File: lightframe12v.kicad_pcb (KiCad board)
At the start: 2 copper layers, 91.4 x 45.7 mm, 46 parts, among them J1 PJ-077, J2 Conn_01x06_Female, J3 Conn_01x06_Female, J4 Conn_01x04_Female, J5 Conn_01x6_Female, Q1 MMBT2222, Q2 MMBT2222, SW1 SW_Push, SW2 SW_Push, U1 ESP32-WROOM-32U, U2 TPS563207s, U3 TLC5971

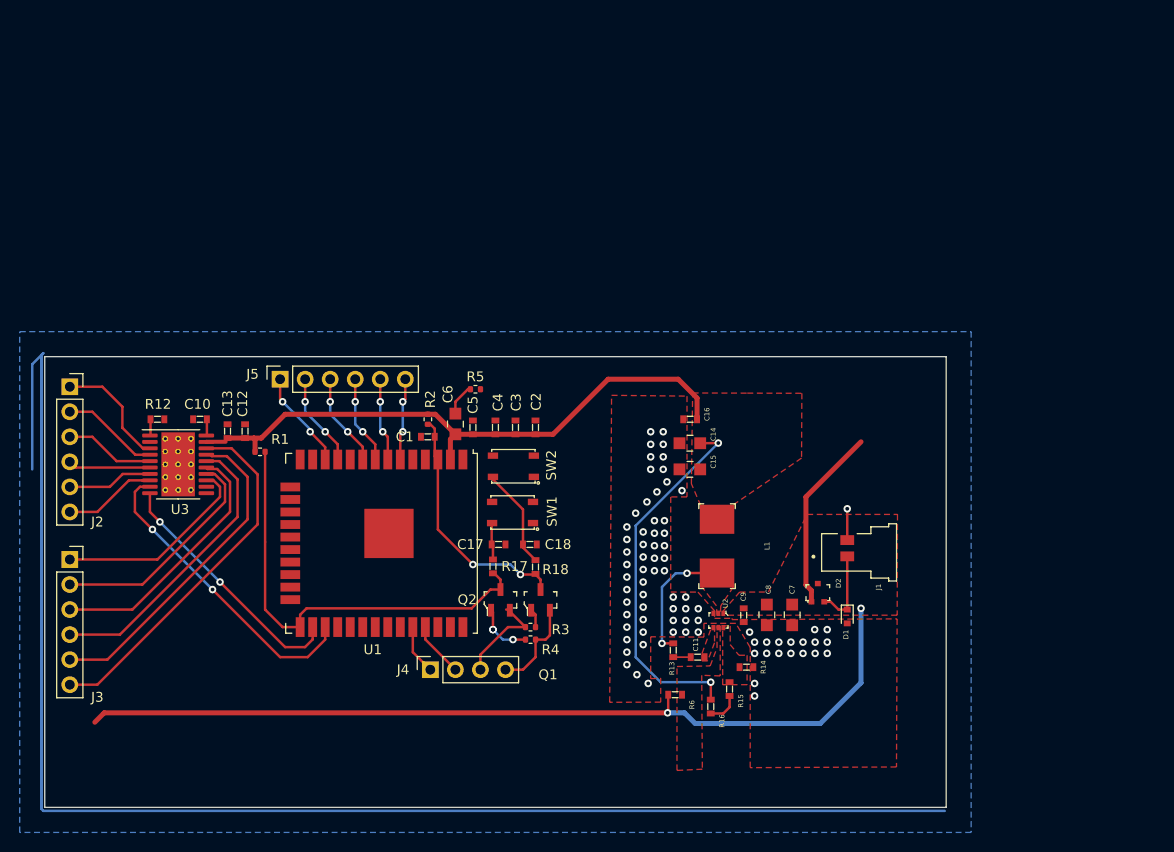
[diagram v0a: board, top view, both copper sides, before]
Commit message: Created pmic footprint
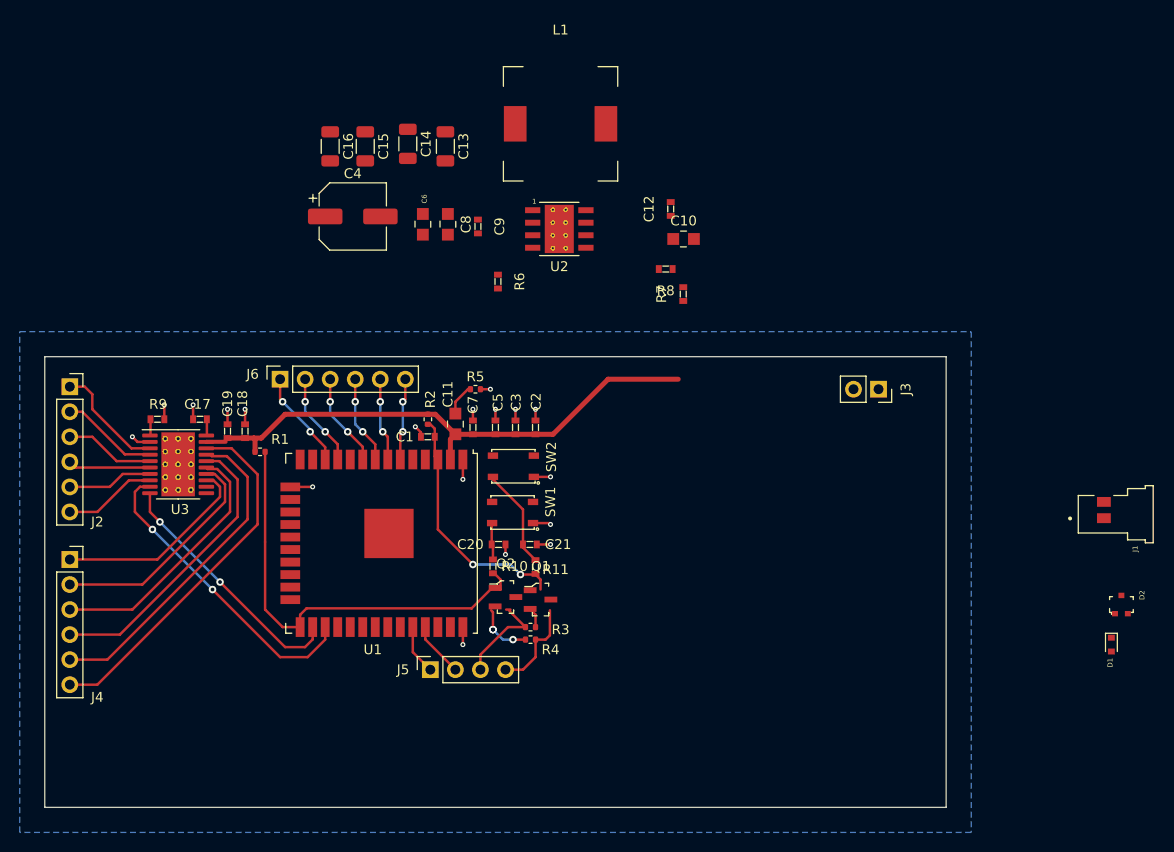
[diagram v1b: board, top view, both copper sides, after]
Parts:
- removed the C11 at (338.0, -508.0)
- removed the C7 at (347.6, -512.3)
- removed R13: 0k, digikey-footprints:0603
- removed R14: 10k, digikey-footprints:0603
- removed R15: 30.9k, digikey-footprints:0603
- removed R16: 51, digikey-footprints:0603
- added C10: 1uF, digikey-footprints:0805, F.Cu at (336.6, -550.4)
- added C12: .1uF, digikey-footprints:0603, F.Cu at (335.3, -553.5)
- added C13: 22uF, Capacitor_SMD:C_1206_3216Metric, F.Cu at (312.4, -559.8)
- added C4: 100uF AL, Capacitor_SMD:CP_Elec_6.3x5.4, F.Cu at (303.0, -552.7)
- added C9: .1uF, digikey-footprints:0603, F.Cu at (315.7, -551.7)
- added J3: Conn_01x02_Female, Connector_PinSocket_2.54mm:PinSocket_1x02_P2.54mm_Vertical, F.Cu at (356.4, -535.2)
- added R7: 100k, digikey-footprints:0603, F.Cu at (336.6, -544.8)
- added R8: 43.2k, digikey-footprints:0603, F.Cu at (334.8, -547.4)
- C14, C15: footprint digikey-footprints:0805 -> Capacitor_SMD:C_1206_3216Metric
- C16: value 100nF -> 22uF; footprint digikey-footprints:0603 -> Capacitor_SMD:C_1206_3216Metric
- C6: renamed from C8; value 10uF -> 4.7uF
- C8: renamed from C9; value 100nF -> 4.7uF; footprint digikey-footprints:0603 -> digikey-footprints:0805
- L1: value 1.2uH -> 8.2uH; footprint keith:Wurth 74437349012 Inductor -> Keith:wurth 7443330820 8.2uH
- Q1, Q2: value MMBT2222 -> MMBT2222A-TP
- U2: value TPS563207s -> LMR33620Simple; footprint digikey-footprints:SOT-563 -> Keith:lmr33620HSOIC
- moved C6 52.8 mm to (310.1, -551.9)
- moved C8 49.7 mm to (312.7, -551.9)
- moved C15 46.5 mm to (304.3, -559.8), turned to 270 degrees
- moved C16 45.8 mm to (300.7, -559.8), turned to 270 degrees
- moved L1 45.7 mm to (324.1, -562.1), turned to 180 degrees
- moved R6 45.6 mm to (317.8, -546.1), turned to 270 degrees
- moved U2 42.9 mm to (324.0, -551.4), turned to 0 degrees
- moved C14 41.7 mm to (308.6, -560.1), turned to 270 degrees
- moved D2 30.8 mm to (381.0, -513.3)
- moved D1 26.9 mm to (380.0, -509.3)
- moved J1 26.3 mm to (380.5, -522.5)
- moved Q2 0.58 mm to (318.5, -514.1), turned to 0 degrees
- turned Q1 to 0 degrees
- renumbered C6 to C11, C10 to C17, C12 to C18, C13 to C19, C17 to C20, C18 to C21, C4 to C5, C5 to C7, J3 to J4, J4 to J5, J5 to J6, R17 to R10, R18 to R11, R12 to R9
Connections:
- C14 pad 2: GND -> Net-(C13-Pad2)
- C15 pad 2: GND -> Net-(C13-Pad2)
- C16 pad 2: GND -> Net-(C13-Pad2)
- C6 pad 1: +12V -> +24V
- C8 pad 1: +12V -> +24V
- D2 pad 1: +12V -> +24V
- L1 pad 1: Net-(L1-Pad1) -> Net-(C12-Pad2)
- Q2 pad 2: /Dtr -> /Gpio0
- Q2 pad 3: /Gpio0 -> /Dtr
- R6 pad 1: +12V -> Net-(R6-Pad1)
- R6 pad 2: Net-(R6-Pad2) -> GND
- U2 pad 1: +12V -> GND
- U2 pad 2: Net-(L1-Pad1) -> +24V
- U2 pad 3: GND -> +24V
- U2 pad 4: Net-(C11-Pad1) -> Net-(R6-Pad1)
- U2 pad 5: Net-(R6-Pad2) -> GND
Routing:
- net (no net): track 196.3 -> 0.00 mm
- net +12V: track 108.4 -> 0.00 mm, vias 2 -> 0
- net +3V3: track 99.3 -> 56.1 mm, vias 2 -> 0
- net GND: track 3.18 -> 26.8 mm, vias 78 -> 18
- net Net-(L1-Pad1): track 13.2 -> 0.00 mm, vias 2 -> 0
- net Net-(D1-Pad1): track 8.06 -> 0.00 mm
- net Net-(R15-Pad2): track 3.31 -> 0.00 mm
- net Net-(C11-Pad2) (its old number): track 1.78 -> 0.00 mm
- removed copper zone on F.Cu, net +12V
- removed copper zone on F.Cu, net +3V3
- removed copper zone on F.Cu, net GND
- removed copper zone on F.Cu, net Net-(C10-Pad1)
- removed copper zone on F.Cu, net Net-(C11-Pad1)
- removed copper zone on F.Cu, net Net-(L1-Pad1)
- removed copper zone on F.Cu, net Net-(R6-Pad2)

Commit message: Rough layout of pmic
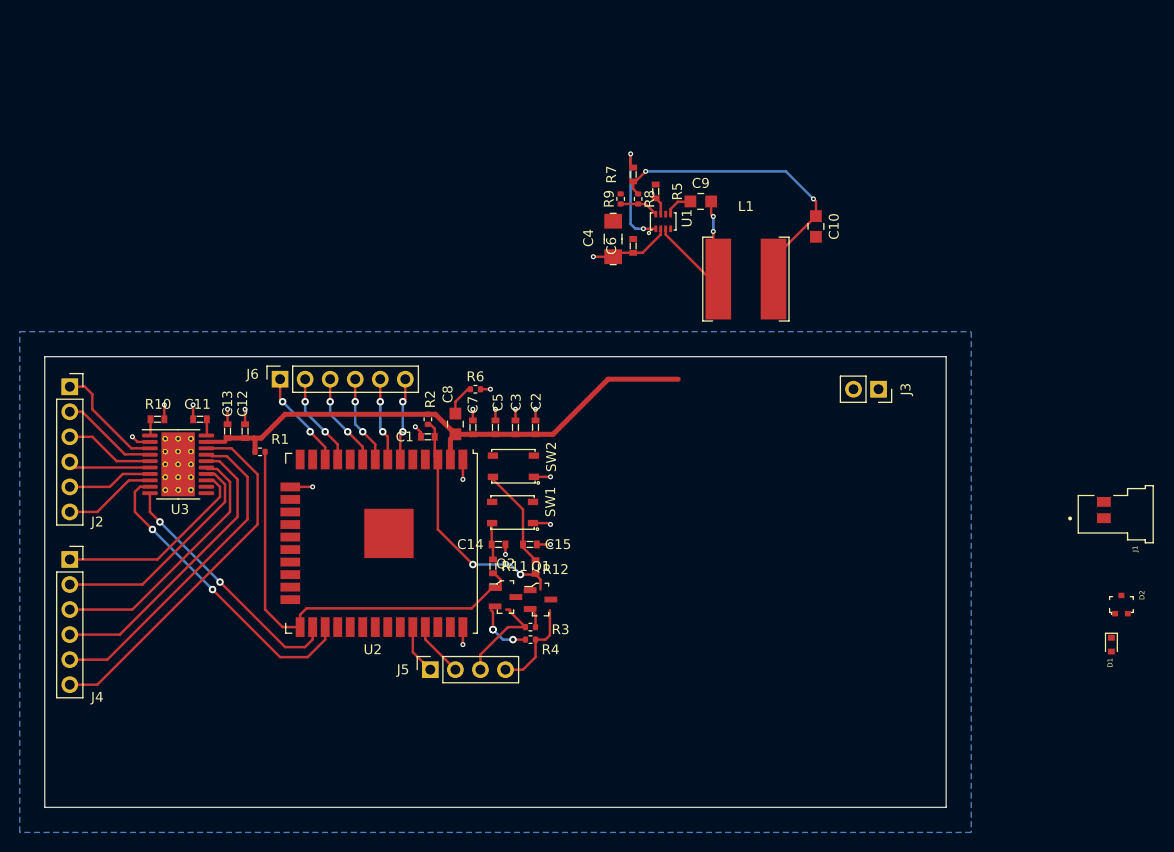
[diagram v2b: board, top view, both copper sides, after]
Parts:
- removed the C12 at (335.3, -553.5)
- removed the C13 at (312.4, -559.8)
- removed the C14 at (308.6, -560.1)
- removed the C15 at (304.3, -559.8)
- removed C16: 22uF, Capacitor_SMD:C_1206_3216Metric
- removed the C4 at (303.0, -552.7)
- removed the C6 at (310.1, -551.9)
- removed the R8 at (334.8, -547.4)
- removed the U2 at (324.0, -551.4)
- added C9: 100nF, digikey-footprints:0805, F.Cu at (338.3, -554.2)
- added R5: 0, digikey-footprints:0603, F.Cu at (333.8, -555.2)
- added R9: 10k, Resistor_SMD:R_0402_1005Metric, F.Cu at (330.2, -554.5)
- added U1: TPS562211, Keith:TPS562211 12V pmic, F.Cu at (334.5, -552.2)
- C10: value 1uF -> 22uF
- C4: renamed from C8; value 4.7uF -> 22uF; footprint digikey-footprints:0805 -> digikey-footprints:1206
- C6: renamed from C9; value .1uF -> 100nF
- L1: value 8.2uH -> 4.7uH; footprint Keith:wurth 7443330820 8.2uH -> Keith:SRN8040 Bournes
- R7: renamed from R6; value 20k -> 10k
- R8: renamed from R7; value 100k -> 45.3k; footprint digikey-footprints:0603 -> Resistor_SMD:R_0402_1005Metric
- moved L1 24.5 mm to (342.9, -546.4), turned to 0 degrees
- moved R7 17.5 mm to (331.5, -557.0), turned to 90 degrees
- moved C4 16.8 mm to (329.4, -550.4), turned to 90 degrees
- moved C6 15.9 mm to (331.5, -549.7), turned to 90 degrees
- moved C10 13.5 mm to (350.0, -551.7), turned to 270 degrees
- moved R8 10.7 mm to (332.0, -554.5), turned to 270 degrees
- renumbered C17 to C11, C18 to C12, C19 to C13, C20 to C14, C21 to C15, C11 to C8, R9 to R10, R10 to R11, R11 to R12, R5 to R6, U1 to U2
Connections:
- net +24V renamed +12V
- C10 pad 1: Net-(C10-Pad1) -> +3V3
- R7 pad 1: Net-(R6-Pad1) -> +3V3
- R7 pad 2: GND -> Net-(R7-Pad2)
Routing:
- net +3V3: track 56.1 -> 87.5 mm, vias 0 -> 2
- net Net-(C9-Pad2): track 0.00 -> 17.0 mm, vias 0 -> 2
- net Net-(R7-Pad2): track 0.00 -> 11.2 mm, vias 0 -> 2
- net +12V: track 0.00 -> 8.36 mm, vias 0 -> 1
- net Net-(R8-Pad2): track 0.00 -> 4.00 mm
- net Net-(C9-Pad1): track 0.00 -> 2.61 mm
- net Net-(R5-Pad2): track 0.00 -> 1.82 mm

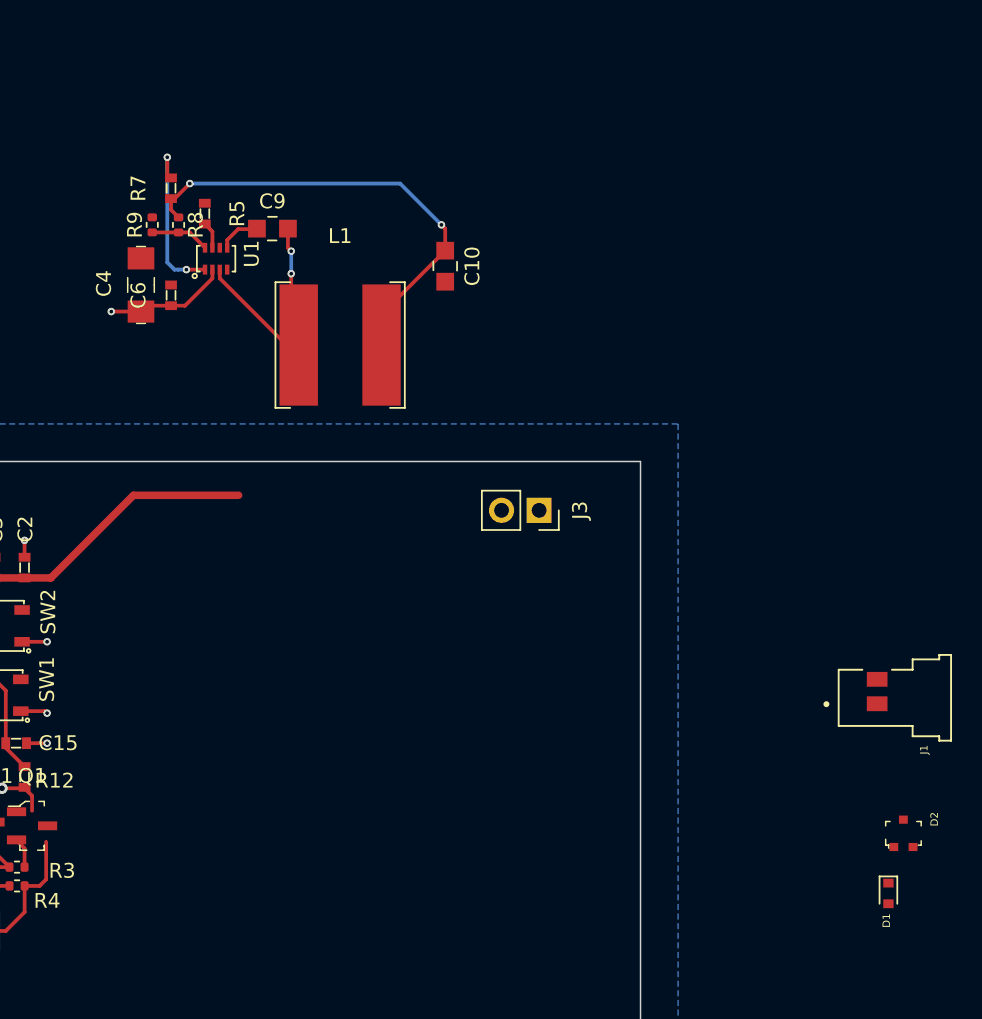
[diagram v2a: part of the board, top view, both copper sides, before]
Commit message: Pmic zones
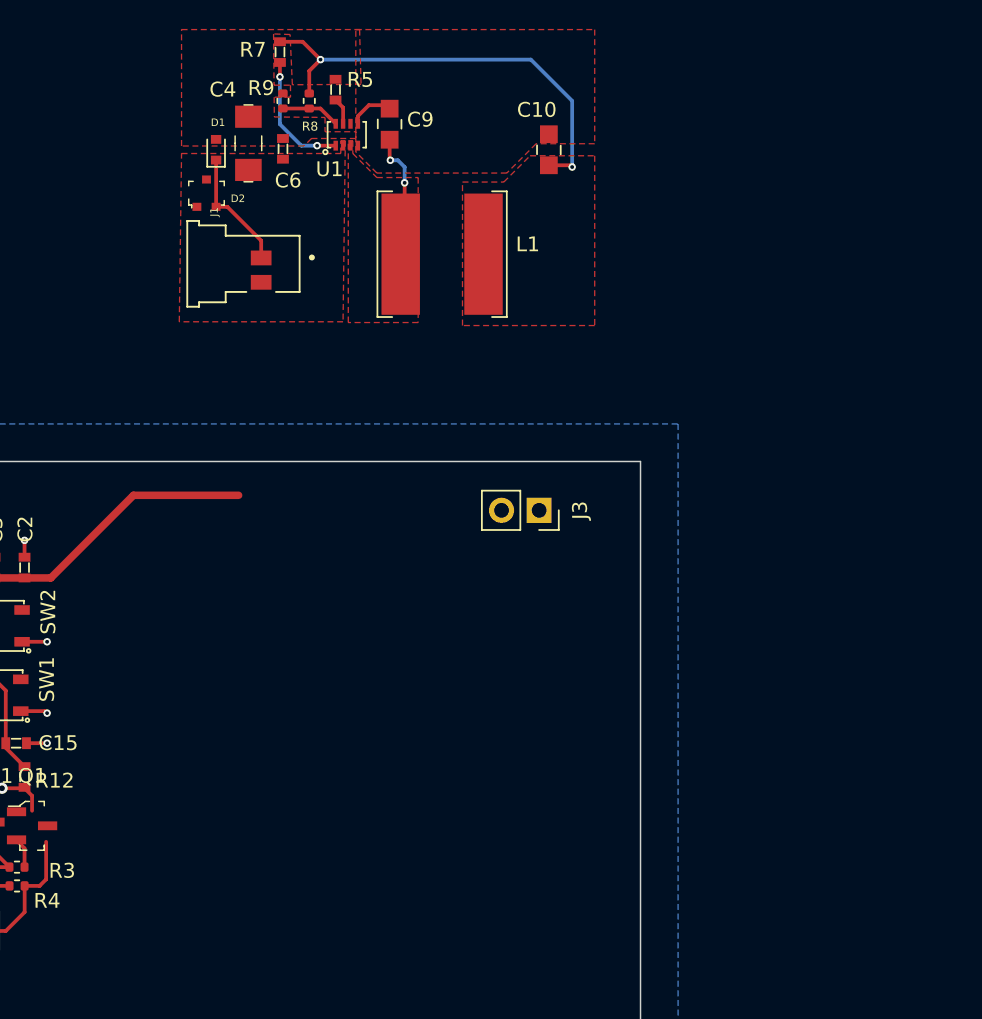
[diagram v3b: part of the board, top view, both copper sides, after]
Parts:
- moved D1 67.8 mm to (334.5, -559.6), turned to 90 degrees
- moved D2 64.0 mm to (333.9, -556.6)
- moved J1 53.1 mm to (336.3, -551.8), turned to 180 degrees
- moved C6 12.5 mm to (339.0, -559.6)
- moved R5 12.2 mm to (342.6, -563.6)
- moved R8 12.2 mm to (340.8, -562.9)
- moved U1 12.2 mm to (343.4, -560.6)
- moved R9 12.2 mm to (339.0, -562.9)
- moved C4 12.0 mm to (336.7, -560.0)
- moved R7 11.8 mm to (338.8, -566.2), turned to 270 degrees
- moved C9 10.6 mm to (346.3, -561.3), turned to 270 degrees
- moved C10 10.5 mm to (357.0, -559.6), turned to 90 degrees
- moved L1 9.24 mm to (349.8, -552.5)
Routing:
- net Net-(C9-Pad2): track 17.0 -> 8.57 mm
- net +12V: track 8.36 -> 0.00 mm, vias 1 -> 0
- net Net-(D1-Pad1): track 0.00 -> 8.32 mm
- net Net-(R7-Pad2): track 11.2 -> 8.55 mm
- net +3V3: track 87.5 -> 86.2 mm
- added copper zone on F.Cu, net +12V
- added copper zone on F.Cu, net +3V3
- added copper zone on F.Cu, net GND
- added copper zone on F.Cu, net Net-(C9-Pad2)

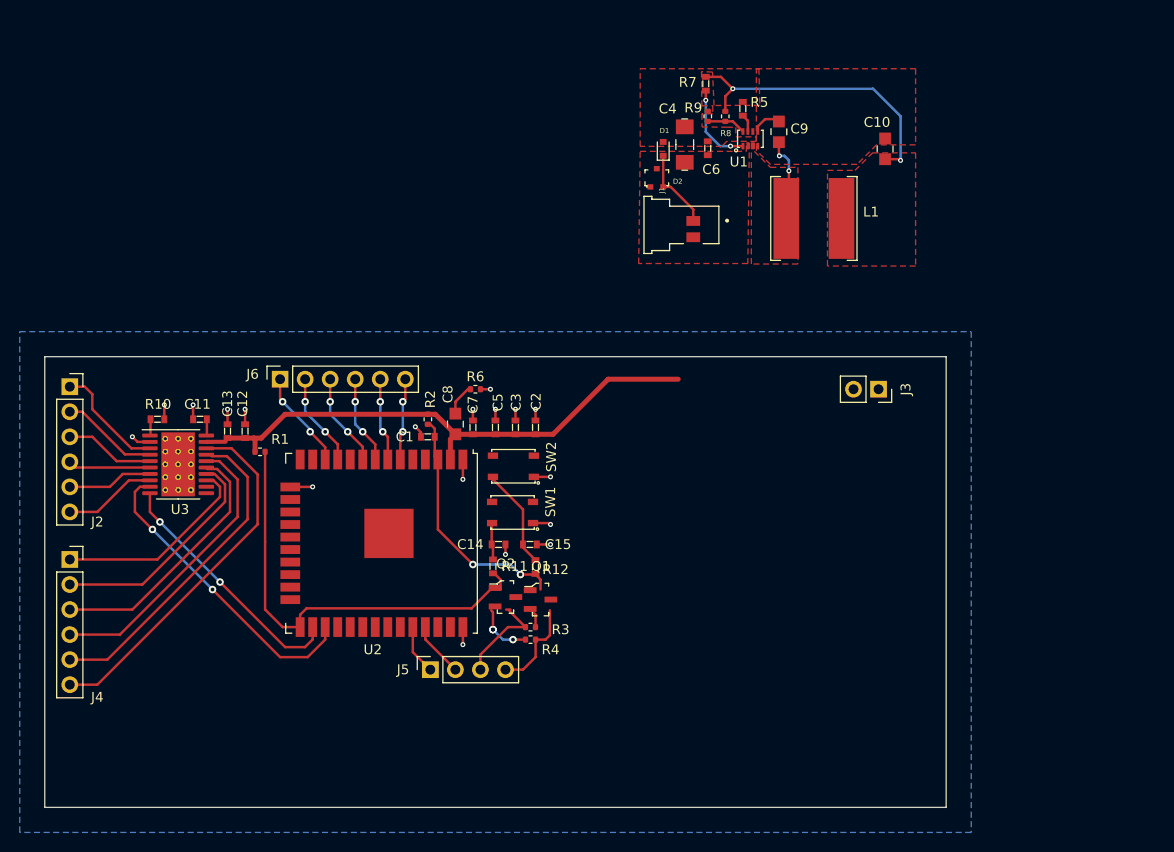
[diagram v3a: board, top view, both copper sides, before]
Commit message: Top ground plane with cutouts.
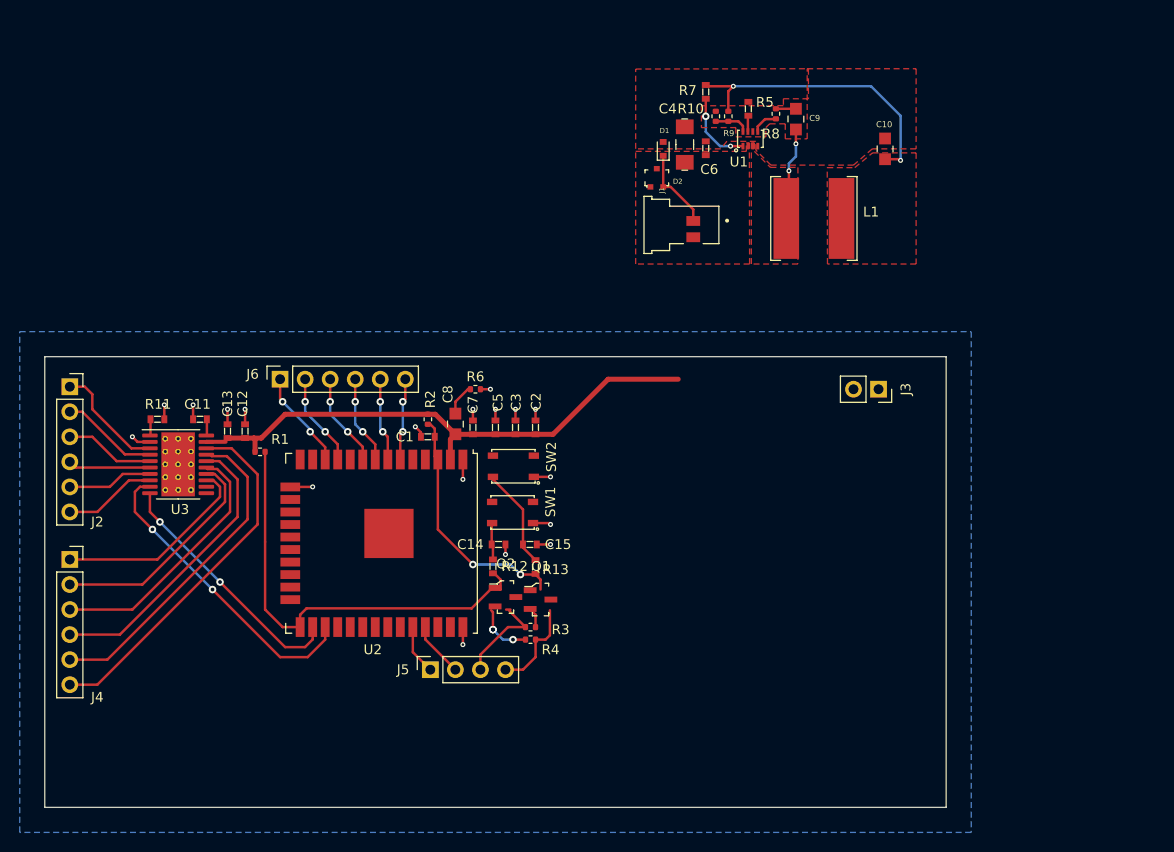
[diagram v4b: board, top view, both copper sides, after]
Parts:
- added R8: 0, Resistor_SMD:R_0402_1005Metric, F.Cu at (345.9, -563.1)
- moved C9 2.15 mm to (348.0, -562.6)
- moved R7 0.82 mm to (338.8, -565.3)
- moved R10 0.81 mm to (339.9, -562.9)
- moved R5 0.56 mm to (343.2, -563.6)
- moved R9 0.30 mm to (341.1, -562.9)
- moved C6 0.20 mm to (338.8, -559.6)
- renumbered R9 to R10, R10 to R11, R11 to R12, R12 to R13, R8 to R9
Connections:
- U1 pad 5: Net-(C9-Pad1) -> Net-(R8-Pad1)
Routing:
- net Net-(R8-Pad1): track 0.00 -> 2.61 mm
- net Net-(C9-Pad2): track 8.57 -> 9.43 mm
- net Net-(R7-Pad2): track 8.55 -> 7.73 mm
- net Net-(C9-Pad1): track 2.61 -> 2.03 mm
